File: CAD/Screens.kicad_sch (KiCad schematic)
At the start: 4 parts, among them J7 RoundDisplay_SPI, J9 RoundDisplay_SPI_v2

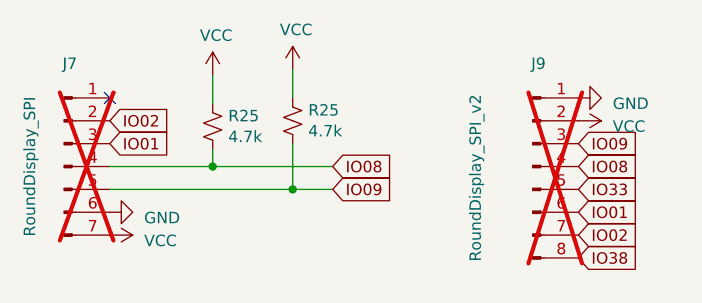
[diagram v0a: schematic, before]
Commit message: Fixed IO pins
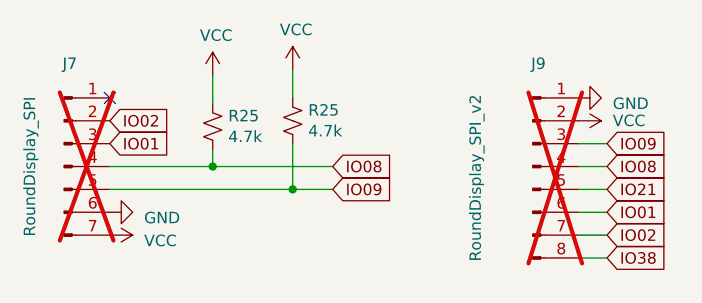
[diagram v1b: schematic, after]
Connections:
- net IO33 renamed IO21
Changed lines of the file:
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@@
+    (stroke (width 0) (type default))
+  )
+  (wire (pts (xy 188.595 85.09) (xy 185.42 85.09))
+    (stroke (width 0) (type default))
+  )
+  (wire (pts (xy 188.595 77.47) (xy 185.42 77.47))
+    (stroke (width 0) (type default))
+  )
+  (wire (pts (xy 188.595 74.93) (xy 185.42 74.93))
     (stroke (width 0) (type default))
   )
@@
     (stroke (width 0) (type default))
   )
+  (wire (pts (xy 188.595 87.63) (xy 185.42 87.63))
+    (stroke (width 0) (type default))
+  )
+  (wire (pts (xy 188.595 82.55) (xy 185.42 82.55))
+    (stroke (width 0) (type default))
+  )
   (wire (pts (xy 158.115 80.01) (xy 153.67 80.01))
     (stroke (width 0) (type default))
@@
     (stroke (width 0) (type default))
   )
+  (wire (pts (xy 188.595 80.01) (xy 185.42 80.01))
+    (stroke (width 0) (type default))
+  )
   (global_label "IO02" (shape input) (at 133.35 72.39 0) (fields_autoplaced)
     (effects (font (size 1.27 1.27)) (justify left))
@@
     )
   )
-  (global_label "IO38" (shape input) (at 185.42 87.63 0) (fields_autoplaced)
+  (global_label "IO38" (shape input) (at 188.595 87.63 0) (fields_autoplaced)
     (effects (font (size 1.27 1.27)) (justify left))
-    (property "Intersheetrefs" "${INTERSHEET_REFS}" (at 192.0259 87.63 0)
+    (property "Intersheetrefs" "${INTERSHEET_REFS}" (at 195.2009 87.63 0)
       (effects (font (size 1.27 1.27)) (justify left) hide)
     )
   )
-  (global_label "IO01" (shape input) (at 185.42 82.55 0) (fields_autoplaced)
+  (global_label "IO21" (shape input) (at 188.595 80.01 0) (fields_autoplaced)
     (effects (font (size 1.27 1.27)) (justify left))
-    (property "Intersheetrefs" "${INTERSHEET_REFS}" (at 192.0259 82.55 0)
+    (property "Intersheetrefs" "${INTERSHEET_REFS}" (at 195.2803 80.01 0)
       (effects (font (size 1.27 1.27)) (justify left) hide)
     )
   )
-  (global_label "IO09" (shape input) (at 185.42 74.93 0) (fields_autoplaced)
+  (global_label "IO01" (shape input) (at 188.595 82.55 0) (fields_autoplaced)
     (effects (font (size 1.27 1.27)) (justify left))
-    (property "Intersheetrefs" "${INTERSHEET_REFS}" (at 192.0259 74.93 0)
+    (property "Intersheetrefs" "${INTERSHEET_REFS}" (at 195.2009 82.55 0)
+      (effects (font (size 1.27 1.27)) (justify left) hide)
+    )
+  )
+  (global_label "IO09" (shape input) (at 188.595 74.93 0) (fields_autoplaced)
+    (effects (font (size 1.27 1.27)) (justify left))
+    (property "Intersheetrefs" "${INTERSHEET_REFS}" (at 195.2009 74.93 0)
       (effects (font (size 1.27 1.27)) (justify left) hide)
     )
@@
     )
   )
-  (global_label "IO08" (shape input) (at 185.42 77.47 0) (fields_autoplaced)
+  (global_label "IO08" (shape input) (at 188.595 77.47 0) (fields_autoplaced)
     (effects (font (size 1.27 1.27)) (justify left))
-    (property "Intersheetrefs" "${INTERSHEET_REFS}" (at 192.0259 77.47 0)
+    (property "Intersheetrefs" "${INTERSHEET_REFS}" (at 195.2009 77.47 0)
       (effects (font (size 1.27 1.27)) (justify left) hide)
     )
@@
     )
   )
-  (global_label "IO33" (shape input) (at 185.42 80.01 0) (fields_autoplaced)
+  (global_label "IO02" (shape input) (at 188.595 85.09 0) (fields_autoplaced)
     (effects (font (size 1.27 1.27)) (justify left))
-    (property "Intersheetrefs" "${INTERSHEET_REFS}" (at 192.0259 80.01 0)
-      (effects (font (size 1.27 1.27)) (justify left) hide)
-    )
-  )
-  (global_label "IO02" (shape input) (at 185.42 85.09 0) (fields_autoplaced)
-    (effects (font (size 1.27 1.27)) (justify left))
-    (property "Intersheetrefs" "${INTERSHEET_REFS}" (at 192.0259 85.09 0)
+    (property "Intersheetrefs" "${INTERSHEET_REFS}" (at 195.2009 85.09 0)
       (effects (font (size 1.27 1.27)) (justify left) hide)
     )
   )
   (symbol (lib_name "VCC_1") (lib_id "power:VCC") (at 185.42 72.39 270) (unit 1)
-    (in_bom yes) (on_board yes) (dnp no) (fields_autoplaced)
+    (in_bom yes) (on_board yes) (dnp no)
     (property "Reference" "#PWR068" (at 181.61 72.39 0)
       (effects (font (size 1.27 1.27)) hide)
     )
-    (property "Value" "VCC" (at 189.23 73.025 90)
+    (property "Value" "VCC" (at 189.23 72.39 90)
       (effects (font (size 1.27 1.27)) (justify left))
     )
